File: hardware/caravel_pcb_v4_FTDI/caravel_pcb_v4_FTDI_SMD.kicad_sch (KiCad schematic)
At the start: 60 parts, among them J1 USB_B_Micro - 10118193-0001LF, J10 Conn_01x27_Female, J11 Conn_01x20_Female, J2 Conn_01x02_Female, J3 Conn_01x02_Male, J4 Conn_01x04_Female, J5 Conn_01x02_Male, J6 Conn_01x02_Male, J7 Conn_01x06_Female, J8 Conn_01x02_Male, J9 Conn_01x02_Male, SW1 SW_Push - SKQGADE010, T1 Logo, T2 Logo, U1 FT232H, U2 SN74LVC1G125DCKR, U3 SN74LVC1G125DCKR, U4 MIC5350-SGYMT-TR, U5 MCP1319MT-29LE-OT, U6 caravel_breakout, U7 W25Q32FVSS, X1 DSC6001_10MHZ, Y1 CSTNE12M0GH5L000R0

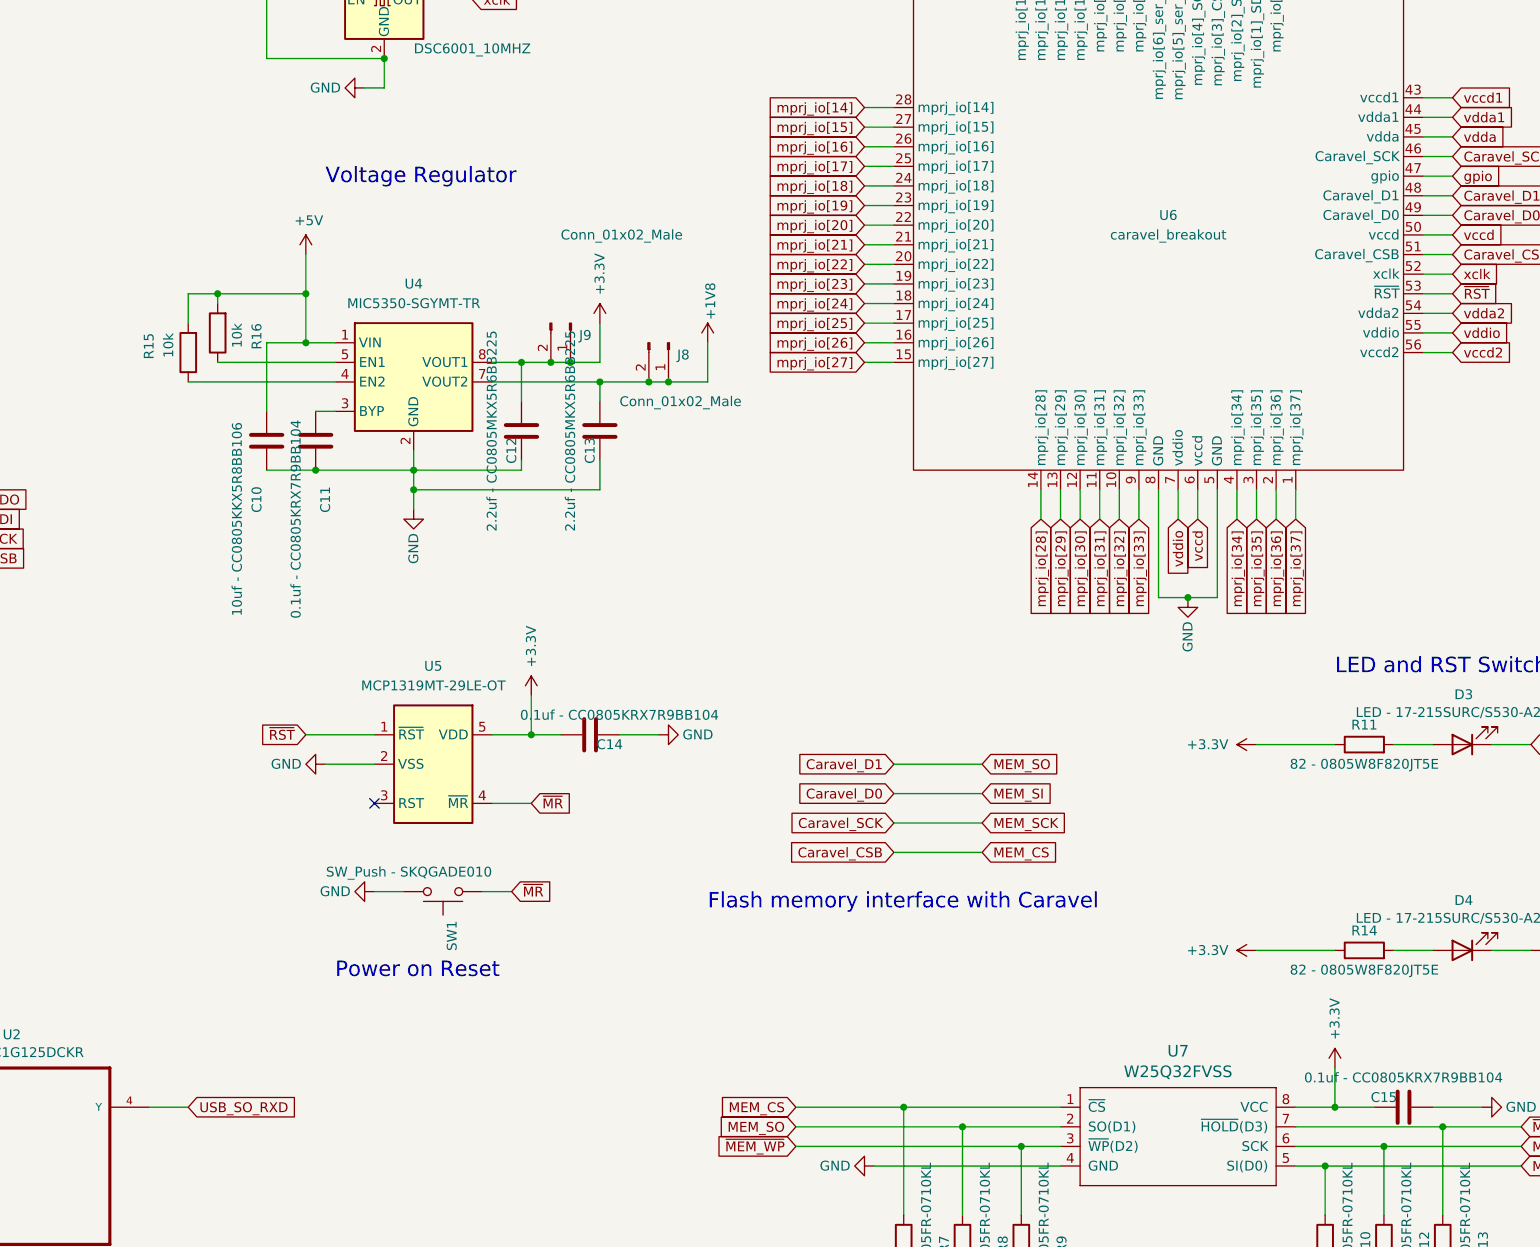
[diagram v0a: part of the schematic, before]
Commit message: update caravel FTDI mainboard V4 (Rev 4B) to support different LDO devices with the same footprint
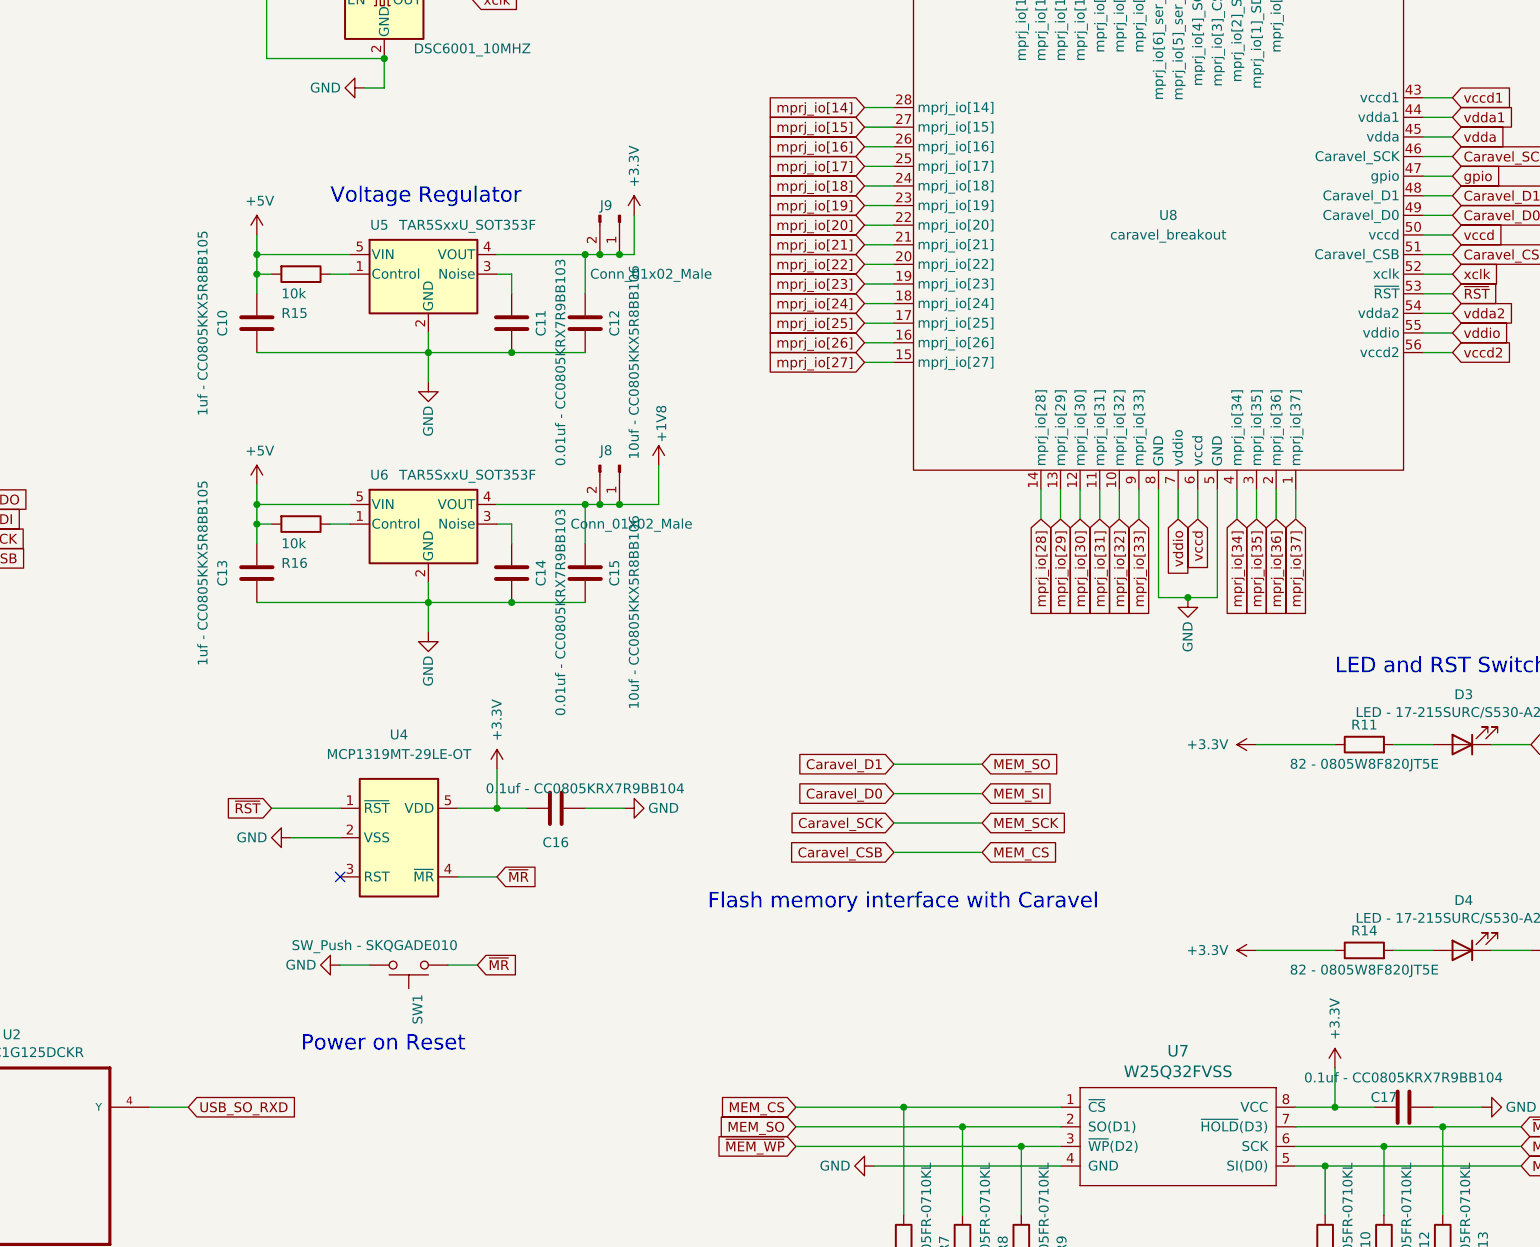
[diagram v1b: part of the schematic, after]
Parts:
- removed U4: MIC5350-SGYMT-TR, Package_DFN_QFN:DFN-8-1EP_2x2mm_P0.5mm_EP0.6x1.2mm, symbol Caravel_board:MIC5350-SGYMT-TR
- removed U5: MCP1319MT-29LE-OT, Caravel_Board:PoR_5_SOT23, symbol Caravel_board:MCP1319MT-29LE-OT
- added C15: 10uf - CC0805KKX5R8BB106, Capacitor_SMD:C_0805_2012Metric, symbol Device:C
- added C16: 0.1uf - CC0805KRX7R9BB104, Capacitor_SMD:C_0805_2012Metric, symbol Device:C
- added U4: MCP1319MT-29LE-OT, Caravel_Board:PoR_5_SOT23, symbol Caravel_board:MCP1319MT-29LE-OT
- added U5, U6: TAR5SxxU_SOT353F, Caravel_Board:SOT-353F, symbol Caravel_board:TAR5SxxU_SOT353F
- C10: value 10uf - CC0805KKX5R8BB106 -> 1uf - CC0805KKX5R8BB105
- C11, C14: value 0.1uf - CC0805KRX7R9BB104 -> 0.01uf - CC0805KRX7R9BB103
- C12: value 2.2uf - CC0805MKX5R6BB225 -> 10uf - CC0805KKX5R8BB106
- C13: value 2.2uf - CC0805MKX5R6BB225 -> 1uf - CC0805KKX5R8BB105
- renumbered C15 to C17, U6 to U8
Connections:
- net +1V8: now also C15.2, U6.4 (VOUT); no longer C13.2
- net +3V3: now also C16.2, U4.5 (VDD), U5.4 (VOUT); no longer C14.2
- net +5V: now also C13.2, U5.5 (VIN), U6.5 (VIN)
- net GND: now also C14.2, C15.1, C16.1, U4.2 (VSS), U5.2 (GND), U6.2 (GND); no longer C14.1
- net ~{MR}: now also U4.4 (~{MR})
- net ~{RST}: now also U4.1 (~{RST})
- net at R16.1: now also U6.1 (Control)
- net at R15.1: now also U5.1 (Control)
- net at C11.1: now also U5.3 (Noise)
- new net: C14.1, U6.3 (Noise)
